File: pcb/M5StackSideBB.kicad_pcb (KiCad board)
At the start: 2 copper layers, 100 x 50 mm, 15 parts, among them J1 Conn_01x14, J2 Conn_01x14, J3 Conn_02x15_Odd_Even, J4 Conn_02x15_Odd_Even

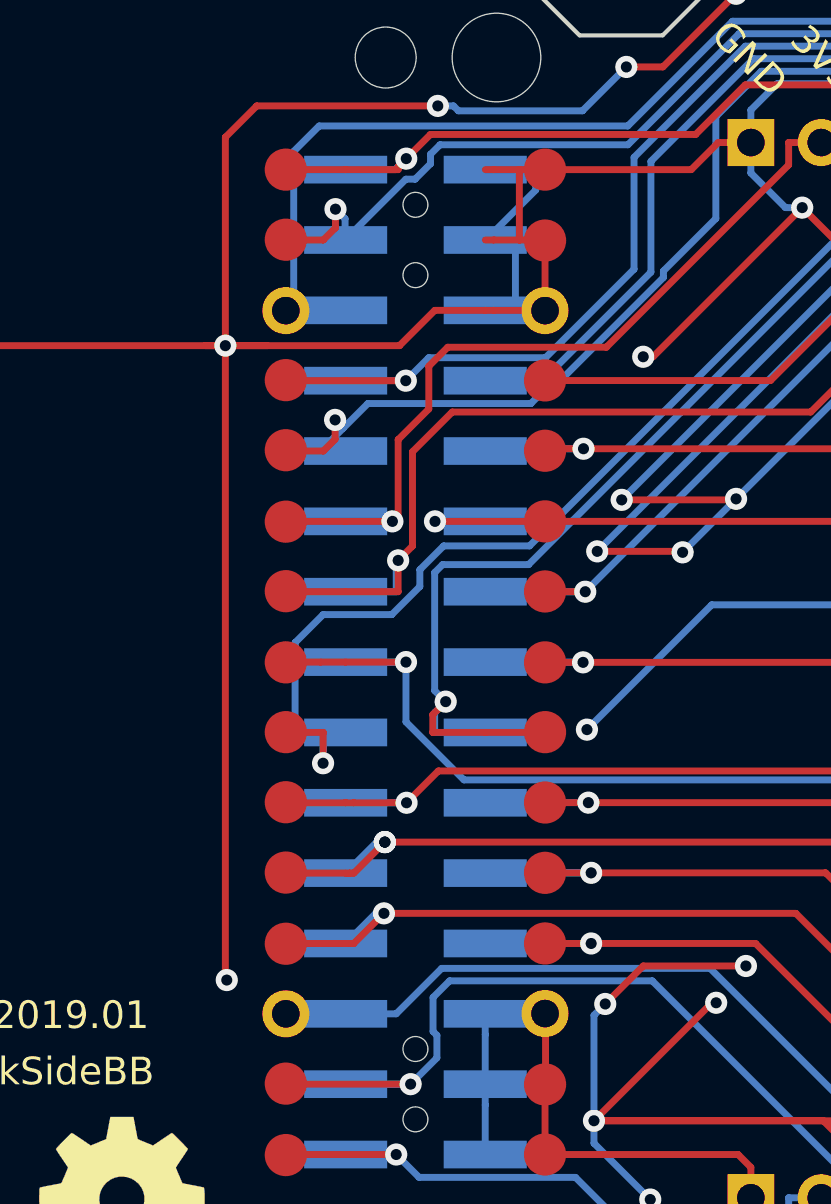
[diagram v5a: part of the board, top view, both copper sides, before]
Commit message: Change footprint for top pad without THT holes
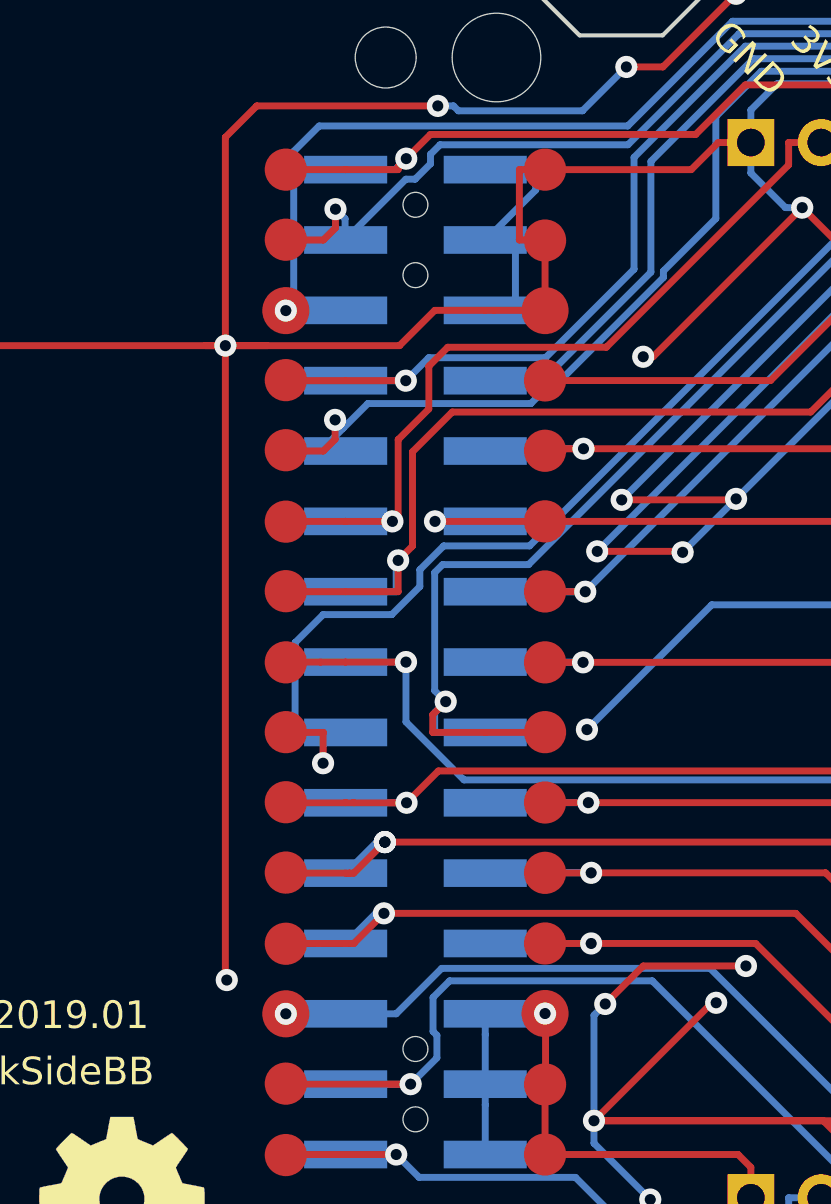
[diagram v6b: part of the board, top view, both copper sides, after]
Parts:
- J3: footprint footprints:PinHeader_2x15_P2.54mm_Vertical_SMD_for_M5Stack_top_only_round_pads -> footprints:PinHeader_2x15_P2.54mm_SMD_pads_only
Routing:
- net GND: track 504.6 -> 502.2 mm
- net RST: track 61.7 -> 63.8 mm, vias 0 -> 1
- net HPWR: vias 0 -> 1
- net G34: vias 0 -> 1

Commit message: Update revision as 2019.03
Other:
- board text added: "Rev 2019.03"
- board text removed: "Rev 2019.01"
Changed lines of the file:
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@@
     (effects (font (size 1 1) (thickness 0.25)))
   )
-  (gr_text "Rev 2019.01" (at 130.0988 87.5792) (layer F.SilkS)
+  (gr_text "Rev 2019.03" (at 130.0988 87.5792) (layer F.SilkS)
     (effects (font (size 1 1) (thickness 0.25)))
   )
@@
     (effects (font (size 1 1) (thickness 0.25)))
   )
-  (gr_text "Rev 2019.01" (at 160.74136 87.86876) (layer B.SilkS)
+  (gr_text "Rev 2019.03" (at 160.74136 87.86876) (layer B.SilkS)
     (effects (font (size 1.2 1.2) (thickness 0.3)) (justify mirror))
   )

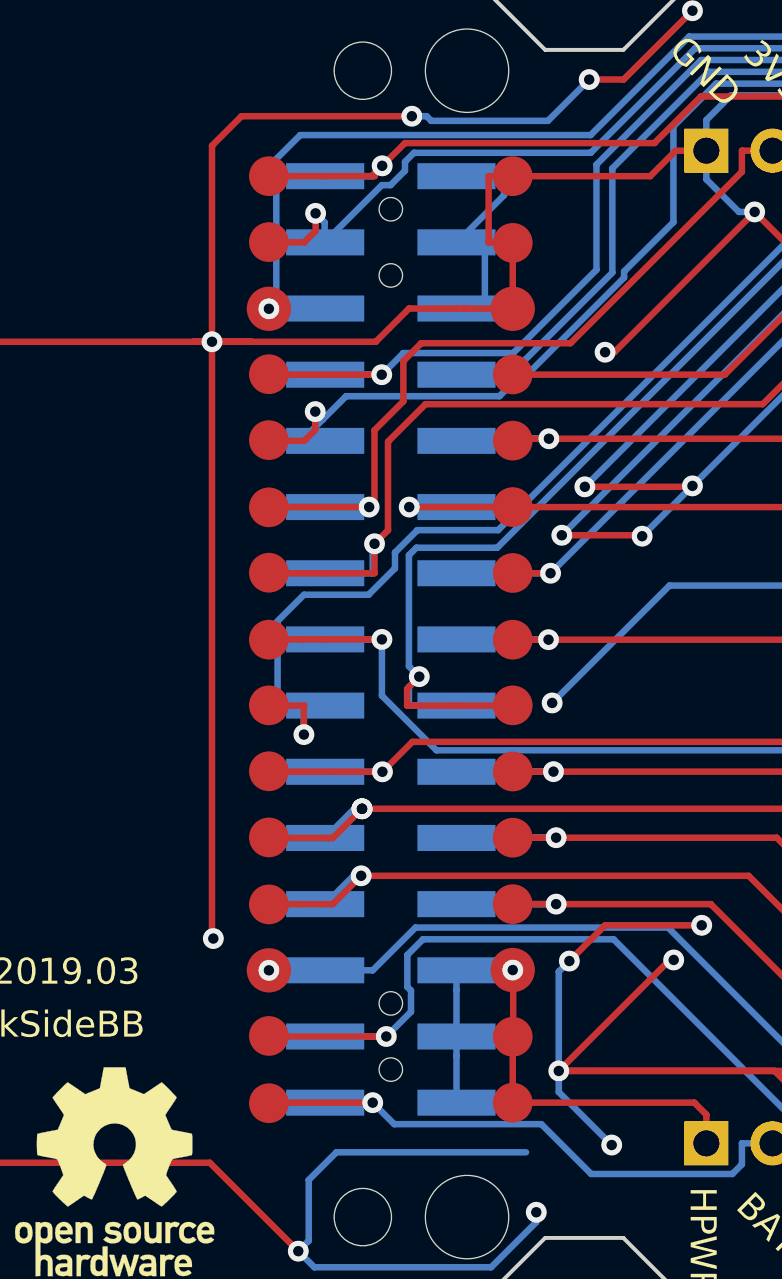
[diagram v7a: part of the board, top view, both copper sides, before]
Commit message: Apply smaller pads for top and bottom
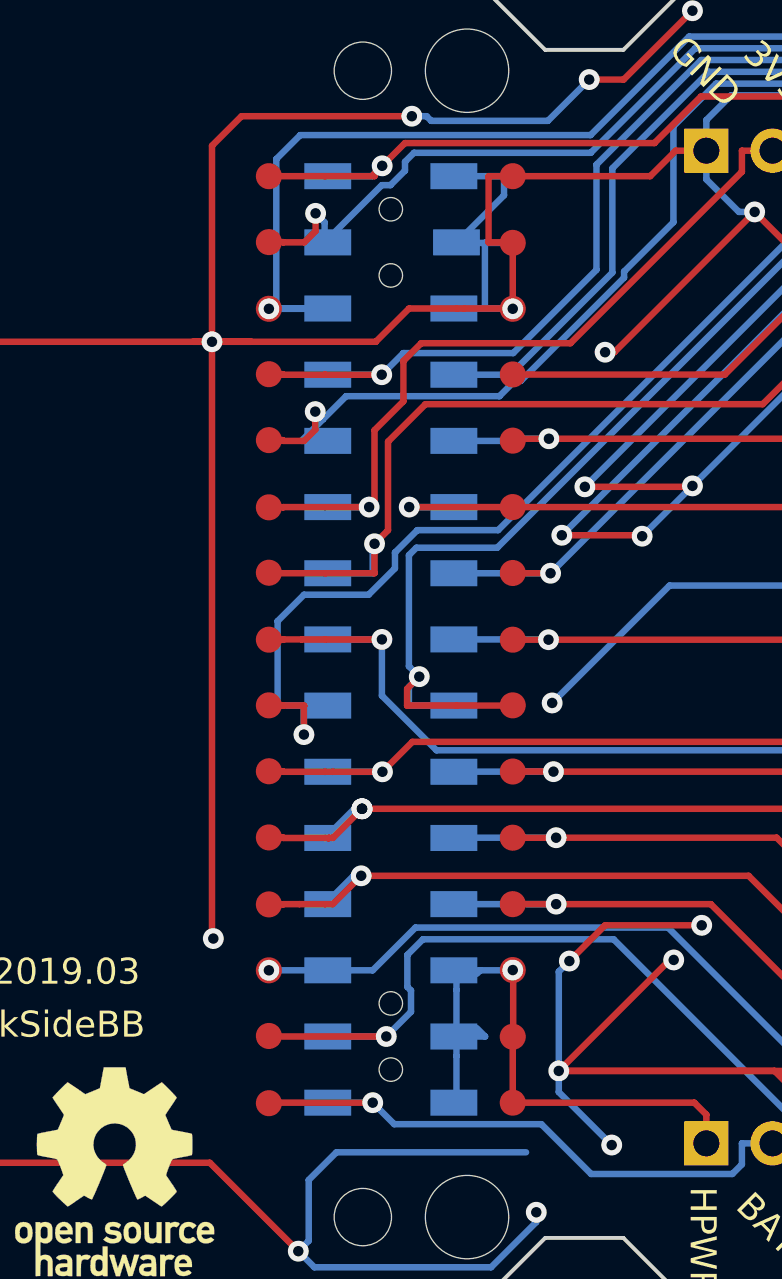
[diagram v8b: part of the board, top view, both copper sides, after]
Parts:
- J4: footprint footprints:PinSocket_2x15_P2.54mm_Vertical_SMD_for_M5Stack_bottom -> footprints:PinSocket_2x15_P2.54mm_Vertical_SMD_just_for_M5Stack_bottom
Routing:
- net GND: vias 32 -> 33
